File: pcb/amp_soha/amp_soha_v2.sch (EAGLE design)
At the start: 55 parts, among them IC1 NE5535U, IC2 7812, IC3 7912, Q1 J113, Q2 J113, Q3 J113, Q4 J113

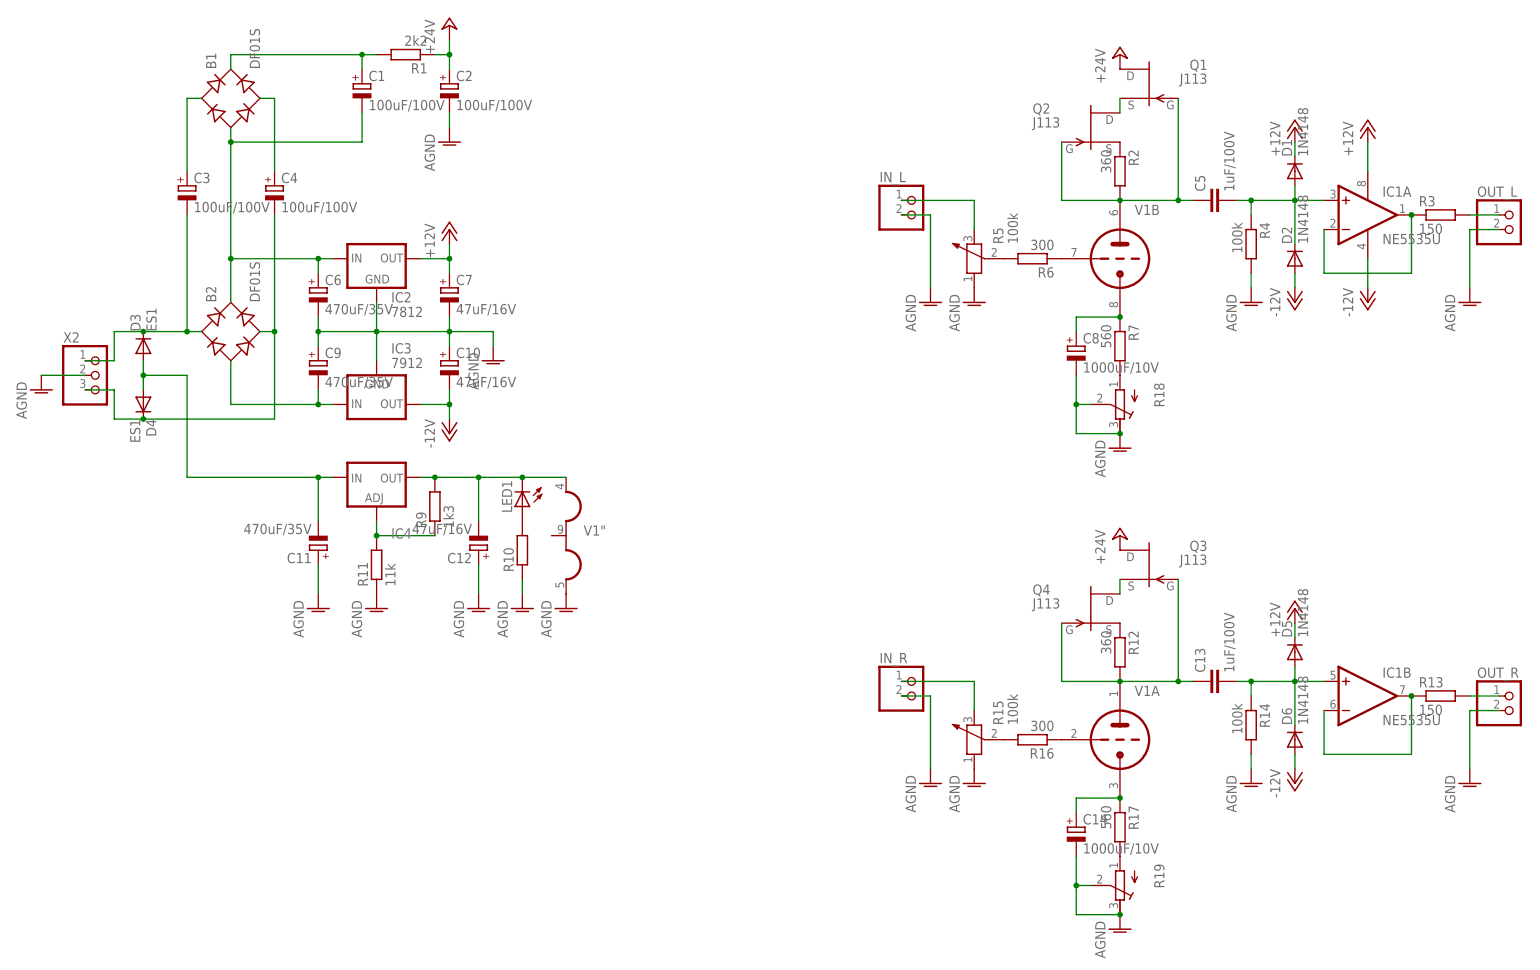
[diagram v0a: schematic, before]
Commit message: 
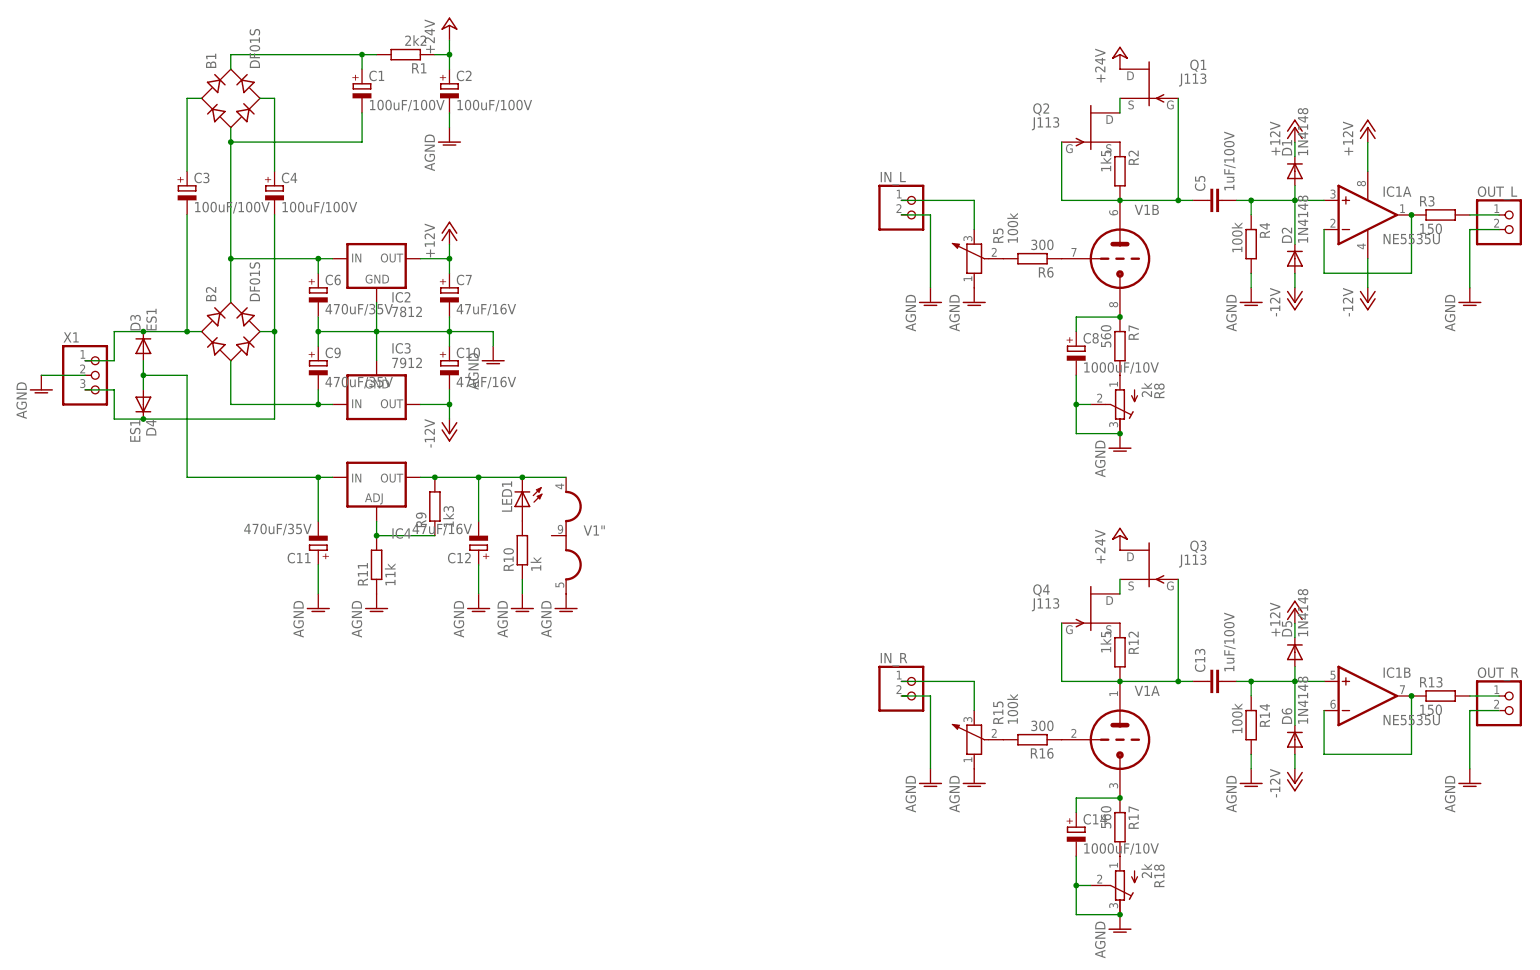
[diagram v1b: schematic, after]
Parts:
- removed R19: (no value), amp_soha:RTRIM329Y
- added R8: 2k, amp_soha:RTRIM329Y
- R10: value (none) -> 1k
- R12, R2: value 360 -> 1k5
- R18: value (none) -> 2k
- renumbered X2 to X1
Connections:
- net AGND: now also R8.E, R8.S; no longer R19.E, R19.S
- net N$17: now also R8.A; no longer R18.A
- net N$18: now also R18.A; no longer R19.A
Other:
- moved on the sheet: R18
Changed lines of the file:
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@@
 <part name="C12" library="amp_soha" deviceset="CPOL-EU" device="E2.5-6" value="47uF/16V"/>
 <part name="AGND4" library="amp_soha" deviceset="AGND" device=""/>
-<part name="R10" library="amp_soha" deviceset="R-EU_" device=""/>
+<part name="R10" library="amp_soha" deviceset="R-EU_" device="" value="1k"/>
 <part name="AGND5" library="amp_soha" deviceset="AGND" device=""/>
 <part name="LED1" library="amp_soha" deviceset="LED" device="5MM"/>
@@
 <part name="C8" library="amp_soha" deviceset="CPOL-EU" device="E5-10,5" value="1000uF/10V"/>
 <part name="AGND11" library="amp_soha" deviceset="AGND" device=""/>
-<part name="R2" library="amp_soha" deviceset="R-EU_" device="" value="360"/>
+<part name="R2" library="amp_soha" deviceset="R-EU_" device="" value="1k5"/>
 <part name="Q2" library="amp_soha" deviceset="J113" device=""/>
 <part name="Q1" library="amp_soha" deviceset="J113" device=""/>
@@
 <part name="C14" library="amp_soha" deviceset="CPOL-EU" device="E5-10,5" value="1000uF/10V"/>
 <part name="AGND16" library="amp_soha" deviceset="AGND" device=""/>
-<part name="R12" library="amp_soha" deviceset="R-EU_" device="" value="360"/>
+<part name="R12" library="amp_soha" deviceset="R-EU_" device="" value="1k5"/>
 <part name="Q4" library="amp_soha" deviceset="J113" device=""/>
 <part name="Q3" library="amp_soha" deviceset="J113" device=""/>
@@
 <part name="AGND18" library="amp_soha" deviceset="AGND" device=""/>
 <part name="IC4" library="amp_soha" deviceset="LM337TS" device=""/>
-<part name="R19" library="amp_soha" deviceset="RTRIM329" device="Y"/>
-<part name="R18" library="amp_soha" deviceset="RTRIM329" device="Y"/>
-<part name="X2" library="amp_soha" deviceset="W237-103" device=""/>
+<part name="R18" library="amp_soha" deviceset="RTRIM329" device="Y" value="2k"/>
+<part name="R8" library="amp_soha" deviceset="RTRIM329" device="Y" value="2k"/>
+<part name="X1" library="amp_soha" deviceset="W237-103" device=""/>
 </parts>
 <sheets>
@@
 <instance part="V1" gate="A" x="185.42" y="-45.72"/>
 <instance part="V1" gate="B" x="185.42" y="38.1"/>
-<instance part="R19" gate="G$1" x="185.42" y="-71.12" rot="R180"/>
-<instance part="R18" gate="G$1" x="185.42" y="12.7" rot="R180"/>
-<instance part="X2" gate="G$1" x="7.62" y="17.78"/>
+<instance part="R18" gate="G$1" x="185.42" y="-71.12" rot="R180"/>
+<instance part="R8" gate="G$1" x="185.42" y="12.7" rot="R180"/>
+<instance part="X1" gate="G$1" x="7.62" y="17.78"/>
 </instances>
 <busses>
@@
 <pinref part="AGND1" gate="VR1" pin="AGND"/>
 <wire x1="5.08" y1="17.78" x2="-2.54" y2="17.78" width="0.1524" layer="91"/>
-<pinref part="X2" gate="G$1" pin="2"/>
+<pinref part="X1" gate="G$1" pin="2"/>
 </segment>
 <segment>
@@
 <wire x1="177.8" y1="12.7" x2="177.8" y2="7.62" width="0.1524" layer="91"/>
 <wire x1="177.8" y1="7.62" x2="185.42" y2="7.62" width="0.1524" layer="91"/>
-<pinref part="R18" gate="G$1" pin="E"/>
+<pinref part="R8" gate="G$1" pin="E"/>
 <junction x="185.42" y="7.62"/>
-<pinref part="R18" gate="G$1" pin="S"/>
+<pinref part="R8" gate="G$1" pin="S"/>
 </segment>
 <segment>
@@
 <wire x1="177.8" y1="-71.12" x2="177.8" y2="-76.2" width="0.1524" layer="91"/>
 <wire x1="177.8" y1="-76.2" x2="185.42" y2="-76.2" width="0.1524" layer="91"/>
-<pinref part="R19" gate="G$1" pin="E"/>
+<pinref part="R18" gate="G$1" pin="E"/>
 <junction x="185.42" y="-76.2"/>
-<pinref part="R19" gate="G$1" pin="S"/>
+<pinref part="R18" gate="G$1" pin="S"/>
 </segment>
 <segment>
@@
 <pinref part="C3" gate="G$1" pin="-"/>
 <wire x1="22.86" y1="45.72" x2="22.86" y2="25.4" width="0.1524" layer="91"/>
-<pinref part="X2" gate="G$1" pin="1"/>
+<pinref part="X1" gate="G$1" pin="1"/>
 </segment>
 </net>
@@
 <pinref part="C4" gate="G$1" pin="-"/>
 <wire x1="38.1" y1="45.72" x2="38.1" y2="25.4" width="0.1524" layer="91"/>
-<pinref part="X2" gate="G$1" pin="3"/>
+<pinref part="X1" gate="G$1" pin="3"/>
 </segment>
 </net>
@@
 <segment>
 <pinref part="R17" gate="G$1" pin="2"/>
-<pinref part="R19" gate="G$1" pin="A"/>
+<pinref part="R18" gate="G$1" pin="A"/>
 </segment>
 </net>
@@
 <segment>
 <pinref part="R7" gate="G$1" pin="2"/>
-<pinref part="R18" gate="G$1" pin="A"/>
-</segment>
-</net>
+<pinref part="R8" gate="G$1" pin="A"/>
+</segment>
+</net>

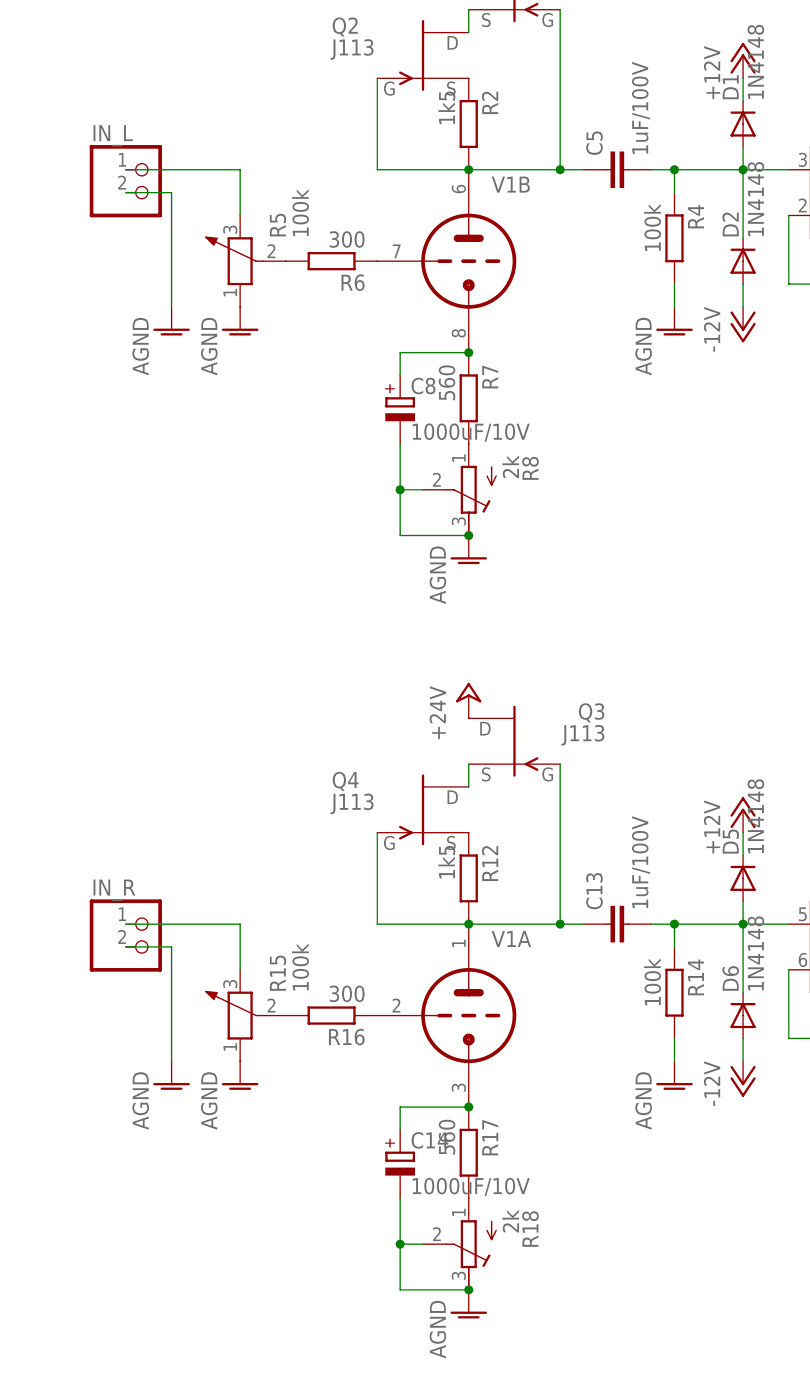
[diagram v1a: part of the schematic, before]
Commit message: 
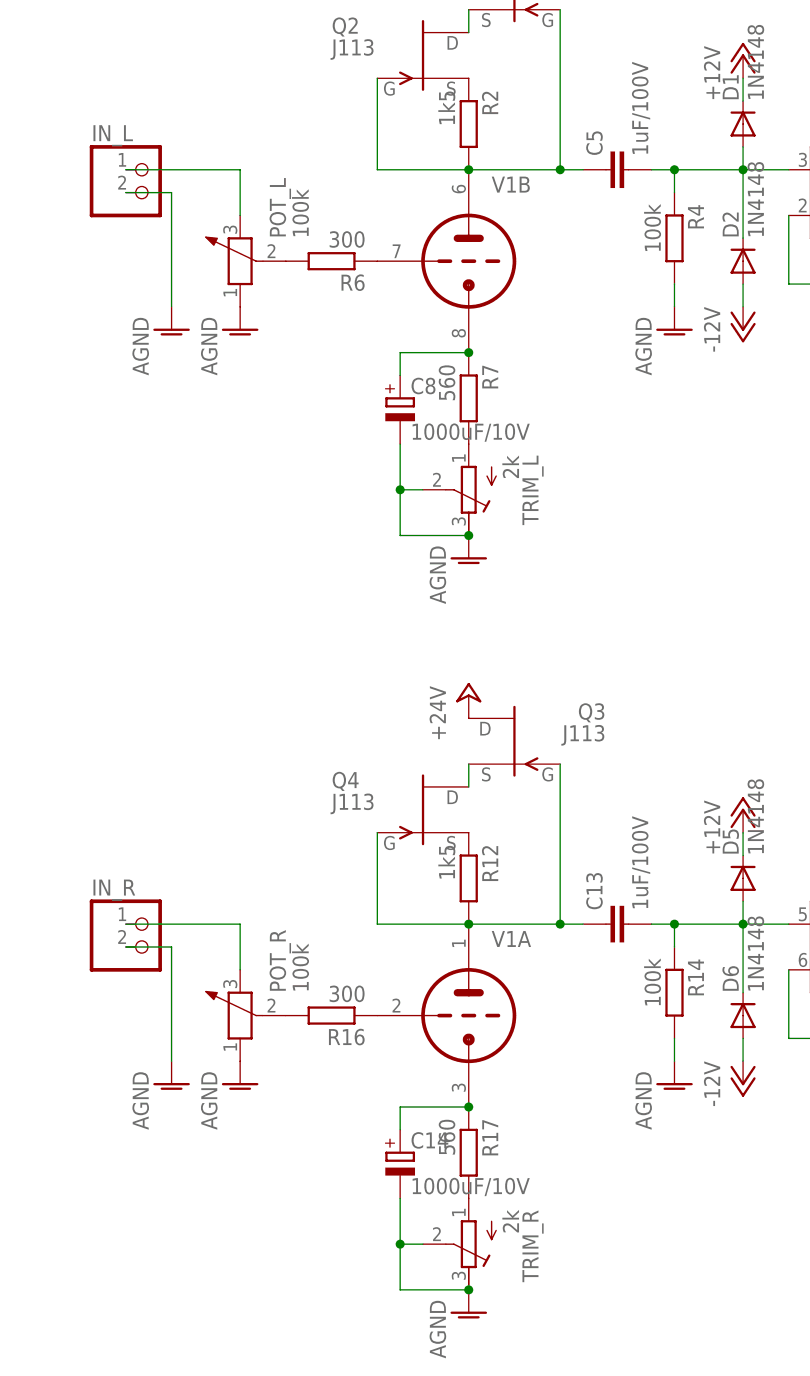
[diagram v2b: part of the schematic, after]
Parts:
- removed R18, R8: 2k, amp_soha:RTRIM329Y
- added TRIM_L, TRIM_R: 2k, amp_soha:RTRIM329W
- renumbered R15 to POT_R, R5 to POT_L
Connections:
- net AGND: now also TRIM_L.E, TRIM_L.S, TRIM_R.E, TRIM_R.S; no longer R18.E, R18.S, R8.E, R8.S
- net N$17: now also TRIM_L.A; no longer R8.A
- net N$18: now also TRIM_R.A; no longer R18.A
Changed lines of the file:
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@@
 <part name="P+2" library="amp_soha" deviceset="+24V" device=""/>
 <part name="IN_L" library="amp_soha" deviceset="PINHD-1X2" device=""/>
-<part name="R5" library="amp_soha" deviceset="POTENTIOMETER_" device="" value="100k"/>
+<part name="POT_L" library="amp_soha" deviceset="POTENTIOMETER_" device="" value="100k"/>
 <part name="AGND9" library="amp_soha" deviceset="AGND" device=""/>
 <part name="AGND10" library="amp_soha" deviceset="AGND" device=""/>
@@
 <part name="AGND13" library="amp_soha" deviceset="AGND" device=""/>
 <part name="IN_R" library="amp_soha" deviceset="PINHD-1X2" device=""/>
-<part name="R15" library="amp_soha" deviceset="POTENTIOMETER_" device="" value="100k"/>
+<part name="POT_R" library="amp_soha" deviceset="POTENTIOMETER_" device="" value="100k"/>
 <part name="AGND14" library="amp_soha" deviceset="AGND" device=""/>
 <part name="AGND15" library="amp_soha" deviceset="AGND" device=""/>
@@
 <part name="AGND18" library="amp_soha" deviceset="AGND" device=""/>
 <part name="IC4" library="amp_soha" deviceset="LM337TS" device=""/>
-<part name="R18" library="amp_soha" deviceset="RTRIM329" device="Y" value="2k"/>
-<part name="R8" library="amp_soha" deviceset="RTRIM329" device="Y" value="2k"/>
+<part name="TRIM_R" library="amp_soha" deviceset="RTRIM329" device="W" value="2k"/>
+<part name="TRIM_L" library="amp_soha" deviceset="RTRIM329" device="W" value="2k"/>
 <part name="X1" library="amp_soha" deviceset="W237-103" device=""/>
 </parts>
@@
 <instance part="P+2" gate="1" x="68.58" y="78.74"/>
 <instance part="IN_L" gate="G$1" x="149.86" y="45.72"/>
-<instance part="R5" gate="1" x="160.02" y="38.1" rot="R90"/>
+<instance part="POT_L" gate="1" x="160.02" y="38.1" rot="R90"/>
 <instance part="AGND9" gate="VR1" x="152.4" y="30.48"/>
 <instance part="AGND10" gate="VR1" x="160.02" y="30.48"/>
@@
 <instance part="AGND13" gate="VR1" x="246.38" y="30.48"/>
 <instance part="IN_R" gate="G$1" x="149.86" y="-38.1"/>
-<instance part="R15" gate="1" x="160.02" y="-45.72" rot="R90"/>
+<instance part="POT_R" gate="1" x="160.02" y="-45.72" rot="R90"/>
 <instance part="AGND14" gate="VR1" x="152.4" y="-53.34"/>
 <instance part="AGND15" gate="VR1" x="160.02" y="-53.34"/>
@@
 <instance part="V1" gate="A" x="185.42" y="-45.72"/>
 <instance part="V1" gate="B" x="185.42" y="38.1"/>
-<instance part="R18" gate="G$1" x="185.42" y="-71.12" rot="R180"/>
-<instance part="R8" gate="G$1" x="185.42" y="12.7" rot="R180"/>
+<instance part="TRIM_R" gate="G$1" x="185.42" y="-71.12" rot="R180"/>
+<instance part="TRIM_L" gate="G$1" x="185.42" y="12.7" rot="R180"/>
 <instance part="X1" gate="G$1" x="7.62" y="17.78"/>
 </instances>
@@
 </segment>
 <segment>
-<pinref part="R5" gate="1" pin="1"/>
+<pinref part="POT_L" gate="1" pin="1"/>
 <pinref part="AGND10" gate="VR1" pin="AGND"/>
 </segment>
@@
 <wire x1="177.8" y1="12.7" x2="177.8" y2="7.62" width="0.1524" layer="91"/>
 <wire x1="177.8" y1="7.62" x2="185.42" y2="7.62" width="0.1524" layer="91"/>
-<pinref part="R8" gate="G$1" pin="E"/>
+<pinref part="TRIM_L" gate="G$1" pin="E"/>
 <junction x="185.42" y="7.62"/>
-<pinref part="R8" gate="G$1" pin="S"/>
+<pinref part="TRIM_L" gate="G$1" pin="S"/>
 </segment>
 <segment>
@@
 </segment>
 <segment>
-<pinref part="R15" gate="1" pin="1"/>
+<pinref part="POT_R" gate="1" pin="1"/>
 <pinref part="AGND15" gate="VR1" pin="AGND"/>
 </segment>
@@
 <wire x1="177.8" y1="-71.12" x2="177.8" y2="-76.2" width="0.1524" layer="91"/>
 <wire x1="177.8" y1="-76.2" x2="185.42" y2="-76.2" width="0.1524" layer="91"/>
-<pinref part="R18" gate="G$1" pin="E"/>
+<pinref part="TRIM_R" gate="G$1" pin="E"/>
 <junction x="185.42" y="-76.2"/>
-<pinref part="R18" gate="G$1" pin="S"/>
+<pinref part="TRIM_R" gate="G$1" pin="S"/>
 </segment>
 <segment>
@@
 <segment>
 <pinref part="IN_L" gate="G$1" pin="1"/>
-<pinref part="R5" gate="1" pin="2"/>
+<pinref part="POT_L" gate="1" pin="2"/>
 <wire x1="147.32" y1="48.26" x2="160.02" y2="48.26" width="0.1524" layer="91"/>
 <wire x1="160.02" y1="48.26" x2="160.02" y2="43.18" width="0.1524" layer="91"/>
@@
 <net name="N$13" class="0">
 <segment>
-<pinref part="R5" gate="1" pin="3"/>
+<pinref part="POT_L" gate="1" pin="3"/>
 <pinref part="R6" gate="G$1" pin="2"/>
 </segment>
@@
 <segment>
 <pinref part="IN_R" gate="G$1" pin="1"/>
-<pinref part="R15" gate="1" pin="2"/>
+<pinref part="POT_R" gate="1" pin="2"/>
 <wire x1="147.32" y1="-35.56" x2="160.02" y2="-35.56" width="0.1524" layer="91"/>
 <wire x1="160.02" y1="-35.56" x2="160.02" y2="-40.64" width="0.1524" layer="91"/>
@@
 <net name="N$27" class="0">
 <segment>
-<pinref part="R15" gate="1" pin="3"/>
+<pinref part="POT_R" gate="1" pin="3"/>
 <pinref part="R16" gate="G$1" pin="2"/>
 </segment>
@@
 <segment>
 <pinref part="R17" gate="G$1" pin="2"/>
-<pinref part="R18" gate="G$1" pin="A"/>
+<pinref part="TRIM_R" gate="G$1" pin="A"/>
 </segment>
 </net>
@@
 <segment>
 <pinref part="R7" gate="G$1" pin="2"/>
-<pinref part="R8" gate="G$1" pin="A"/>
-</segment>
-</net>
+<pinref part="TRIM_L" gate="G$1" pin="A"/>
+</segment>
+</net>
